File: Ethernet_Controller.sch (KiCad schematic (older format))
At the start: 45 parts, among them J1 WE-RJ45_7499111121A, T1 749020010A, U1 RTL8111H, Y1 ECS-1618-250-BN-TR

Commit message: Add review comments
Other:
- note added: "Ethernet connector have built in magnetics. \nIs using separate transformer intentional?\nUse connector without magnetics or change to connector \nwith magnetics and POE"
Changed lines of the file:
@@
 Text Label 6600 8400 2    50   ~ 0
 ETH_1V0
+Text Notes 6600 900  0    50   ~ 0
+Ethernet connector have built in magnetics. \nIs using separate transformer intentional?\nUse connector without magnetics or change to connector \nwith magnetics and POE
 $EndSCHEMATC

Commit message: fixed clock connections
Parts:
- removed C10, C9: C_10p_0402, antmicro-footprints:0402-cap, symbol antmicroCapacitors0402:C_10p_0402
- removed R17: R_1M0_0402, antmicro-footprints:0402-res, symbol antmicroResistors0402:R_1M0_0402
- removed Y1: ECS-1618-250-BN-TR, antmicro-footprints:OSC_ECS-1618-250-BN-TR, symbol antmicroOscillators:ECS-1618-250-BN-TR
- added C? (x2): C_10p_0402, antmicro-footprints:0402-cap, symbol antmicroCapacitors0402:C_10p_0402
- added R?: R_1M0_0402, antmicro-footprints:0402-res, symbol antmicroResistors0402:R_1M0_0402
- added Y?: ABM8G-25.000MHZ-18-D2Y-T, antmicro-footprints:KX-7, symbol antmicroCrystals:ABM8G-25.000MHZ-18-D2Y-T
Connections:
- wire segments 184 -> 185
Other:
- note removed: "Review Oscillator connection."
- note removed: "Why is this 1M resistor here? \n"
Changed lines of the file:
@@
 Text Notes 1600 950  0    50   ~ 0
 Choke is on secondary side.\n(Where only data is passed through)
-Wire Wire Line
-	6800 4600 6350 4600
-Wire Wire Line
-	6350 4600 6350 4450
-Wire Wire Line
-	8400 4800 8400 4950
-$Comp
-L power:GND #PWR07
-U 1 1 6199D143
-P 8400 4950
-F 0 "#PWR07" H 8400 4700 50  0001 C CNN
-F 1 "GND" H 8405 4777 50  0000 C CNN
-F 2 "" H 8400 4950 50  0001 C CNN
-F 3 "" H 8400 4950 50  0001 C CNN
-	1    8400 4950
-	1    0    0    -1
-$EndComp
 $Comp
 L antmicroResistors0402:R_1k_0402 R10
@@
 PCIE1_RX_N
 $Comp
-L antmicroOscillators:ECS-1618-250-BN-TR Y1
-U 1 1 61A23266
-P 7000 4200
-F 0 "Y1" H 7600 4549 50  0000 C CNN
-F 1 "ECS-1618-250-BN-TR" H 7600 4458 50  0000 C CNN
-F 2 "antmicro-footprints:OSC_ECS-1618-250-BN-TR" H 7000 4200 50  0001 C CNN
-F 3 "https://ecsxtal.com/store/pdf/ECS_1618.pdf" H 7000 4200 50  0001 C CNN
-F 4 "ECS-1618-250-BN-TR" H 7600 4367 50  0000 C CNN "MPN"
-F 5 "ECSXTAL" H 7600 4276 50  0000 C CNN "Manufacturer"
-	1    7000 4200
-	1    0    0    -1
-$EndComp
-Text Notes 9950 4750 0    50   ~ 0
-Review Oscillator connection.
-Text Label 9750 4500 0    50   ~ 0
-XTAL2
-Wire Wire Line
-	9500 4500 9750 4500
-Wire Wire Line
-	8700 4500 8950 4500
-Text Label 8700 4500 0    50   ~ 0
-XTAL1
-Wire Wire Line
-	9500 4500 9500 4550
-Connection ~ 9500 4500
-Wire Wire Line
-	9400 4500 9500 4500
-Wire Wire Line
-	8950 4500 9100 4500
-$Comp
-L antmicroResistors0402:R_1M0_0402 R17
-U 1 1 619ADB78
-P 9250 4500
-F 0 "R17" H 9250 4713 60  0000 C CNN
-F 1 "R_1M0_0402" H 9250 4350 60  0001 C CNN
-F 2 "antmicro-footprints:0402-res" H 9450 4700 60  0001 L CNN
-F 3 "" H 9250 4500 50  0001 C CNN
-F 4 "TE CONNECTIVITY" H 9450 4900 60  0001 L CNN "Manufacturer"
-F 5 "CRG0402F1M0" H 9450 4800 60  0001 L CNN "MPN"
-F 6 "1M0" H 9250 4615 50  0000 C CNN "Val"
-	1    9250 4500
-	1    0    0    -1
-$EndComp
-Wire Wire Line
-	8950 4500 8950 4550
-Connection ~ 8950 4500
-$Comp
-L power:GND #PWR011
-U 1 1 619A95EF
-P 9500 4850
-F 0 "#PWR011" H 9500 4600 50  0001 C CNN
-F 1 "GND" H 9505 4677 50  0000 C CNN
-F 2 "" H 9500 4850 50  0001 C CNN
-F 3 "" H 9500 4850 50  0001 C CNN
-	1    9500 4850
-	1    0    0    -1
-$EndComp
-$Comp
-L antmicroCapacitors0402:C_10p_0402 C10
-U 1 1 619A945F
-P 9500 4700
-F 0 "C10" H 9615 4745 60  0000 L CNN
-F 1 "C_10p_0402" H 9500 4550 60  0001 C CNN
-F 2 "antmicro-footprints:0402-cap" H 9700 4900 60  0001 L CNN
-F 3 "" H 9500 4700 50  0001 C CNN
-F 4 "MULTICOMP" H 9700 5100 60  0001 L CNN "Manufacturer"
-F 5 "MC0402N100D500CT" H 9700 5000 60  0001 L CNN "MPN"
-F 6 "10p" H 9615 4647 50  0000 L CNN "Val"
-	1    9500 4700
-	1    0    0    -1
-$EndComp
-$Comp
-L power:GND #PWR08
-U 1 1 619A53C6
-P 8950 4850
-F 0 "#PWR08" H 8950 4600 50  0001 C CNN
-F 1 "GND" H 8955 4677 50  0000 C CNN
-F 2 "" H 8950 4850 50  0001 C CNN
-F 3 "" H 8950 4850 50  0001 C CNN
-	1    8950 4850
-	1    0    0    -1
-$EndComp
-$Comp
-L antmicroCapacitors0402:C_10p_0402 C9
-U 1 1 619A5032
-P 8950 4700
-F 0 "C9" H 9065 4745 60  0000 L CNN
-F 1 "C_10p_0402" H 8950 4550 60  0001 C CNN
-F 2 "antmicro-footprints:0402-cap" H 9150 4900 60  0001 L CNN
-F 3 "" H 8950 4700 50  0001 C CNN
-F 4 "MULTICOMP" H 9150 5100 60  0001 L CNN "Manufacturer"
-F 5 "MC0402N100D500CT" H 9150 5000 60  0001 L CNN "MPN"
-F 6 "10p" H 9065 4647 50  0000 L CNN "Val"
-	1    8950 4700
-	1    0    0    -1
-$EndComp
-Wire Wire Line
-	8950 4400 8950 4500
-Text Notes 8950 4200 0    50   ~ 0
-Why is this 1M resistor here? \n
-Wire Wire Line
-	9500 3850 6800 3850
-Wire Wire Line
-	6800 3850 6800 4400
-Wire Wire Line
-	9500 3850 9500 4500
-Wire Wire Line
-	8400 4400 8950 4400
-$Comp
 L antmicroResistors0402:R_2k49_1%_0402 R5
 U 1 1 61B0F054
@@
 Text GLabel 7500 5350 1    50   Input ~ 0
 3V3
-Text GLabel 6350 4450 1    50   Input ~ 0
-1V8
 $Comp
 L antmicroInterfaceControllers:RTL8111H U1
@@
 Text Notes 6600 900  0    50   ~ 0
 Ethernet connector have built in magnetics. \nIs using separate transformer intentional?\nUse connector without magnetics or change to connector \nwith magnetics and POE
+$Comp
+L antmicroCrystals:ABM8G-25.000MHZ-18-D2Y-T Y?
+U 1 1 6246C7D0
+P 7700 4250
+F 0 "Y?" H 7550 4450 31  0000 L CNN
+F 1 "ABM8G-25.000MHZ-18-D2Y-T" H 7750 4450 31  0000 L CNN
+F 2 "antmicro-footprints:KX-7" H 9800 4250 50  0001 C CNN
+F 3 "" H 9900 4350 50  0001 C CNN
+F 4 "ABM8G-25.000MHZ-18-D2Y-T" H 7894 4219 31  0001 L CNN "MPN"
+F 5 "Abracon" H 7894 4157 31  0001 L CNN "Manufacturer"
+	1    7700 4250
+	1    0    0    -1
+$EndComp
+Wire Wire Line
+	7550 4250 7150 4250
+Wire Wire Line
+	7850 4250 8300 4250
+Text Label 7150 4250 0    50   ~ 0
+XTAL1
+Text Label 8300 4250 2    50   ~ 0
+XTAL2
+$Comp
+L antmicroCapacitors0402:C_10p_0402 C?
+U 1 1 6248C548
+P 7150 4500
+F 0 "C?" H 7265 4545 60  0000 L CNN
+F 1 "C_10p_0402" H 7150 4350 60  0001 C CNN
+F 2 "antmicro-footprints:0402-cap" H 7350 4700 60  0001 L CNN
+F 3 "" H 7150 4500 50  0001 C CNN
+F 4 "MULTICOMP" H 7350 4900 60  0001 L CNN "Manufacturer"
+F 5 "MC0402N100D500CT" H 7350 4800 60  0001 L CNN "MPN"
+F 6 "10p" H 7265 4447 50  0000 L CNN "Val"
+	1    7150 4500
+	1    0    0    -1
+$EndComp
+$Comp
+L antmicroCapacitors0402:C_10p_0402 C?
+U 1 1 6248CDDF
+P 8300 4500
+F 0 "C?" H 8415 4545 60  0000 L CNN
+F 1 "C_10p_0402" H 8300 4350 60  0001 C CNN
+F 2 "antmicro-footprints:0402-cap" H 8500 4700 60  0001 L CNN
+F 3 "" H 8300 4500 50  0001 C CNN
+F 4 "MULTICOMP" H 8500 4900 60  0001 L CNN "Manufacturer"
+F 5 "MC0402N100D500CT" H 8500 4800 60  0001 L CNN "MPN"
+F 6 "10p" H 8415 4447 50  0000 L CNN "Val"
+	1    8300 4500
+	1    0    0    -1
+$EndComp
+Wire Wire Line
+	7150 4250 7150 4350
+Wire Wire Line
+	8300 4250 8300 4350
+Wire Wire Line
+	7700 4050 7700 4000
+Wire Wire Line
+	7700 4450 7700 4700
+$Comp
+L power:GND #PWR?
+U 1 1 624B2B57
+P 7700 4800
+F 0 "#PWR?" H 7700 4550 50  0001 C CNN
+F 1 "GND" H 7705 4627 50  0000 C CNN
+F 2 "" H 7700 4800 50  0001 C CNN
+F 3 "" H 7700 4800 50  0001 C CNN
+	1    7700 4800
+	1    0    0    -1
+$EndComp
+$Comp
+L power:GND #PWR?
+U 1 1 624B3561
+P 7700 4000
+F 0 "#PWR?" H 7700 3750 50  0001 C CNN
+F 1 "GND" H 7705 3827 50  0000 C CNN
+F 2 "" H 7700 4000 50  0001 C CNN
+F 3 "" H 7700 4000 50  0001 C CNN
+	1    7700 4000
+	-1   0    0    1
+$EndComp
+Wire Wire Line
+	7150 4250 7150 3700
+Wire Wire Line
+	7150 3700 7550 3700
+Wire Wire Line
+	8300 3700 8300 4250
+Connection ~ 7150 4250
+Connection ~ 8300 4250
+$Comp
+L antmicroResistors0402:R_1M0_0402 R?
+U 1 1 624BEECF
+P 7700 3700
+F 0 "R?" H 7700 3900 60  0000 C CNN
+F 1 "R_1M0_0402" H 7700 3550 60  0001 C CNN
+F 2 "antmicro-footprints:0402-res" H 7900 3900 60  0001 L CNN
+F 3 "" H 7700 3700 50  0001 C CNN
+F 4 "TE CONNECTIVITY" H 7900 4100 60  0001 L CNN "Manufacturer"
+F 5 "CRG0402F1M0" H 7900 4000 60  0001 L CNN "MPN"
+F 6 "1M0" H 7700 3800 50  0000 C CNN "Val"
+F 7 "DNP" H 7700 3700 50  0000 C CNN "DNP"
+	1    7700 3700
+	1    0    0    -1
+$EndComp
+Wire Wire Line
+	7850 3700 8300 3700
+Wire Wire Line
+	7150 4650 7150 4700
+Wire Wire Line
+	7150 4700 7700 4700
+Connection ~ 7700 4700
+Wire Wire Line
+	7700 4700 7700 4800
+Wire Wire Line
+	7700 4700 8300 4700
+Wire Wire Line
+	8300 4700 8300 4650
 $EndSCHEMATC

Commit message: annotations
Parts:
- gave numbers to parts that had none: 16
- renumbered C5 to C11, C6 to C13, C7 to C14, C8 to C16, C2 to C7, C3 to C8, C4 to C9, R9 to R10, R10 to R11, R11 to R12, R12 to R13, R13 to R14, R14 to R16, R15 to R17, R16 to R18, R6 to R7, R7 to R8, R8 to R9

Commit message: Add local libs to fix CI
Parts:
- C1, C13: footprint antmicro-footprints:1210-cap -> sa800u-baseboard-hw-footprints:1210-cap; symbol antmicroCapacitorsmisc:C_1n_1210_2kV -> sa800u-baseboard-hw:C_1n_1210_2kV
- C10, C12, C15, C17, C18, C2, C3, C6, C7, C8: footprint antmicro-footprints:0402-cap -> sa800u-baseboard-hw-footprints:0402-cap; symbol antmicroCapacitors0402:C_100n_0402 -> sa800u-baseboard-hw:C_100n_0402
- C11, C14, C16, C9: footprint antmicro-footprints:0402-cap -> sa800u-baseboard-hw-footprints:0402-cap; symbol antmicroCapacitors0402:C_10n_0402 -> sa800u-baseboard-hw:C_10n_0402
- C19: footprint antmicro-footprints:0402-cap -> sa800u-baseboard-hw-footprints:0402-cap; symbol antmicroCapacitors0402:C_1u_0402 -> sa800u-baseboard-hw:C_1u_0402
- C20, C21: footprint antmicro-footprints:0402-cap -> sa800u-baseboard-hw-footprints:0402-cap; symbol antmicroCapacitors0402:C_10p_0402 -> sa800u-baseboard-hw:C_10p_0402
- C4, C5: footprint antmicro-footprints:0402-cap -> sa800u-baseboard-hw-footprints:0402-cap; symbol antmicroCapacitors0402:C_4u7_0402 -> sa800u-baseboard-hw:C_4u7_0402
- D1, D2: footprint antmicro-footprints:SOT-23-3 -> sa800u-baseboard-hw-footprints:SOT-23-3; symbol antmicroDiodesZenerSingle:BZX84C6V2LT1G -> sa800u-baseboard-hw:BZX84C6V2LT1G
- J1: footprint antmicro-footprints:7499111121A -> sa800u-baseboard-hw-footprints:7499111121A; symbol antmicroModularConnectorsJacksWithMagnetics:WE-RJ45_7499111121A -> sa800u-baseboard-hw:WE-RJ45_7499111121A
- R1, R10, R2, R3, R4, R7, R8, R9: footprint antmicro-footprints:0402-res -> sa800u-baseboard-hw-footprints:0402-res; symbol antmicroResistors0402:R_75R_0402 -> sa800u-baseboard-hw:R_75R_0402
- R11, R14: footprint antmicro-footprints:0402-res -> sa800u-baseboard-hw-footprints:0402-res; symbol antmicroResistors0402:R_1k_0402 -> sa800u-baseboard-hw:R_1k_0402
- R12, R13: footprint antmicro-footprints:0402-res -> sa800u-baseboard-hw-footprints:0402-res; symbol antmicroResistors0402:R_10k_0402 -> sa800u-baseboard-hw:R_10k_0402
- R15: footprint antmicro-footprints:0402-res -> sa800u-baseboard-hw-footprints:0402-res; symbol antmicroResistors0402:R_1M0_0402 -> sa800u-baseboard-hw:R_1M0_0402
- R16: footprint antmicro-footprints:0603-res -> sa800u-baseboard-hw-footprints:0603-res; symbol antmicroResistors0603:R_15k_0603 -> sa800u-baseboard-hw:R_15k_0603
- R17, R18: footprint antmicro-footprints:0402-res -> sa800u-baseboard-hw-footprints:0402-res; symbol antmicroResistors0402:R_470R_0402 -> sa800u-baseboard-hw:R_470R_0402
- R5: footprint antmicro-footprints:0402-res -> sa800u-baseboard-hw-footprints:0402-res; symbol antmicroResistors0402:R_2k49_1%_0402 -> sa800u-baseboard-hw:R_2k49_1%_0402
- R6: footprint antmicro-footprints:0402-res -> sa800u-baseboard-hw-footprints:0402-res; symbol antmicroResistors0402:R_0R_0402 -> sa800u-baseboard-hw:R_0R_0402
- T1: footprint antmicro-footprints:749020010A -> sa800u-baseboard-hw-footprints:749020010A; symbol antmicroInterfaceDriversReceiversTransceivers:749020010A -> sa800u-baseboard-hw:749020010A
- U1: footprint antmicro-footprints:RTL8111H -> sa800u-baseboard-hw-footprints:RTL8111H; symbol antmicroInterfaceControllers:RTL8111H -> sa800u-baseboard-hw:RTL8111H
- Y1: footprint antmicro-footprints:KX-7 -> sa800u-baseboard-hw-footprints:KX-7; symbol antmicroCrystals:ABM8G-25.000MHZ-18-D2Y-T -> sa800u-baseboard-hw:ABM8G-25.000MHZ-18-D2Y-T

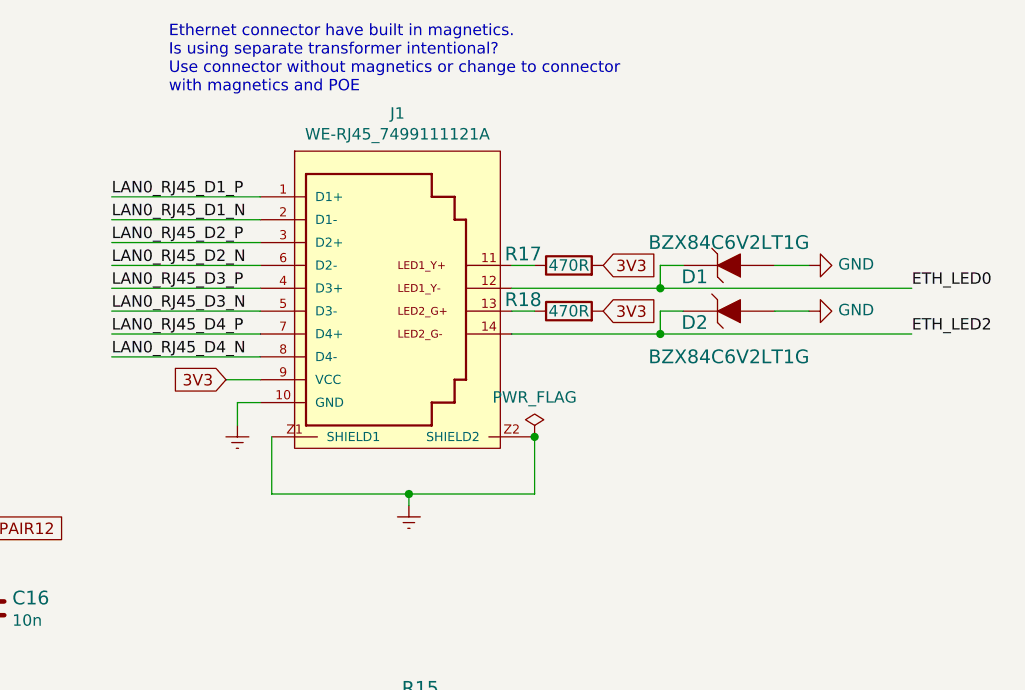
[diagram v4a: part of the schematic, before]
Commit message: add rj45 without trafo
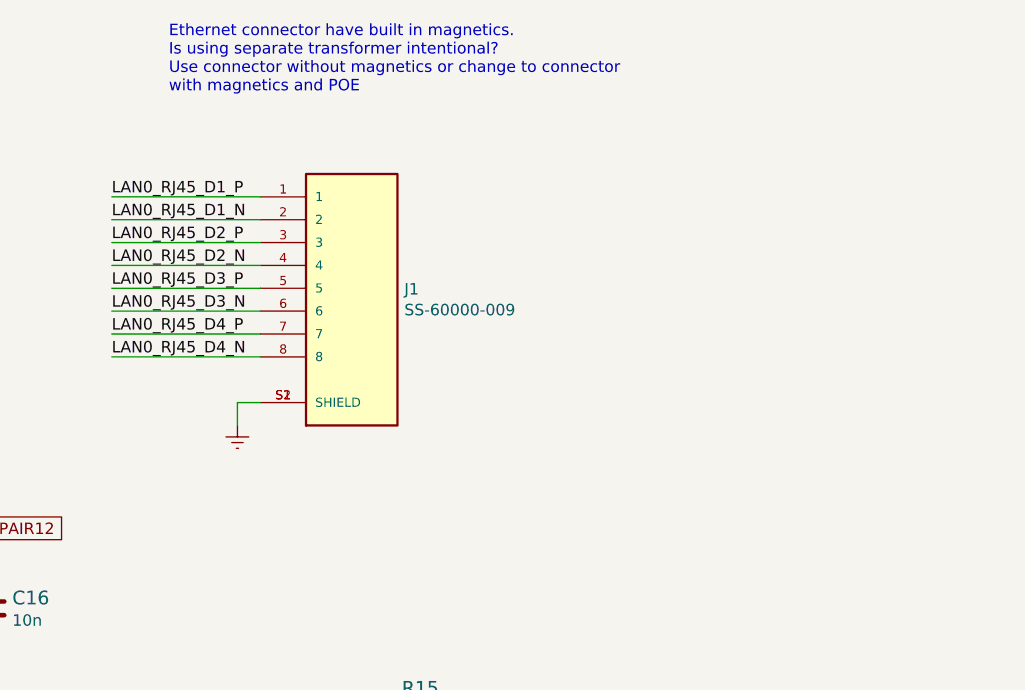
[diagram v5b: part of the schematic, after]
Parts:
- removed D1, D2: BZX84C6V2LT1G, sa800u-baseboard-hw-footprints:SOT-23-3, symbol sa800u-baseboard-hw:BZX84C6V2LT1G
- removed J1: WE-RJ45_7499111121A, sa800u-baseboard-hw-footprints:7499111121A, symbol sa800u-baseboard-hw:WE-RJ45_7499111121A
- removed R17, R18: R_470R_0402, sa800u-baseboard-hw-footprints:0402-res, symbol sa800u-baseboard-hw:R_470R_0402
- added J1: SS-60000-009, antmicro-footprints:BEL_SS-60000-009, symbol antmicroModularConnectorsJacks:SS-60000-009
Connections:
- net Earth: now also J1.S1 (SHIELD), J1.S2 (SHIELD)
- net LAN0_RJ45_D1_N: now also J1.2
- net LAN0_RJ45_D1_P: now also J1.1
- net LAN0_RJ45_D2_N: now also J1.4
- net LAN0_RJ45_D2_P: now also J1.3
- net LAN0_RJ45_D3_N: now also J1.6
- net LAN0_RJ45_D3_P: now also J1.5
- net LAN0_RJ45_D4_N: now also J1.8
- net LAN0_RJ45_D4_P: now also J1.7
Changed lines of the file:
@@
 	2050 2100 2800 2100
-Wire Wire Line
-	9250 1850 9400 1850
-Wire Wire Line
-	9250 1650 9400 1650
-Wire Wire Line
-	8200 2650 8200 2400
-Wire Wire Line
-	7050 2400 7050 2650
-Text GLabel 6850 2150 0    50   Input ~ 0
-3V3
-Text Label 9850 1950 0    50   ~ 0
-ETH_LED2
-$Comp
-L sa800u-baseboard-hw:BZX84C6V2LT1G D2
-U 1 1 61991971
-P 9050 1850
-F 0 "D2" H 9200 1900 60  0000 C CNN
-F 1 "BZX84C6V2LT1G" H 9050 2050 60  0000 C CNN
-F 2 "sa800u-baseboard-hw-footprints:SOT-23-3" H 9250 2050 60  0001 L CNN
-F 3 "https://www.onsemi.com/pdf/datasheet/bzx84c2v4lt1-d.pdf" H 9250 2150 60  0001 L CNN
-F 4 "BZX84C6V2LT1G" H 9250 2350 60  0001 L CNN "MPN"
-F 5 "ON Semiconductor" H 9250 2950 60  0001 L CNN "Manufacturer"
-	1    9050 1850
-	-1   0    0    1
-$EndComp
-Connection ~ 8750 1750
-Wire Wire Line
-	8750 1650 8750 1750
-Wire Wire Line
-	8850 1650 8750 1650
-Wire Wire Line
-	8100 1750 8750 1750
-Wire Wire Line
-	8750 1850 8850 1850
-Wire Wire Line
-	8750 1950 8750 1850
-Wire Wire Line
-	8100 1950 8750 1950
-Text GLabel 8500 1850 2    50   Input ~ 0
-3V3
-Text GLabel 8500 1650 2    50   Input ~ 0
-3V3
-$Comp
-L sa800u-baseboard-hw:BZX84C6V2LT1G D1
-U 1 1 61976A91
-P 9050 1650
-F 0 "D1" H 9200 1700 60  0000 C CNN
-F 1 "BZX84C6V2LT1G" H 9050 1550 60  0000 C CNN
-F 2 "sa800u-baseboard-hw-footprints:SOT-23-3" H 9250 1850 60  0001 L CNN
-F 3 "https://www.onsemi.com/pdf/datasheet/bzx84c2v4lt1-d.pdf" H 9250 1950 60  0001 L CNN
-F 4 "BZX84C6V2LT1G" H 9250 2150 60  0001 L CNN "MPN"
-F 5 "ON Semiconductor" H 9250 2750 60  0001 L CNN "Manufacturer"
-	1    9050 1650
-	-1   0    0    1
-$EndComp
-Wire Wire Line
-	8200 1850 8100 1850
-Text Label 9850 1750 0    50   ~ 0
-ETH_LED0
-Wire Wire Line
-	8100 1650 8200 1650
-$Comp
-L sa800u-baseboard-hw:R_470R_0402 R17
-U 1 1 6196D91A
-P 8350 1650
-F 0 "R17" H 8150 1700 60  0000 C CNN
-F 1 "R_470R_0402" H 8350 1500 60  0001 C CNN
-F 2 "sa800u-baseboard-hw-footprints:0402-res" H 8550 1850 60  0001 L CNN
-F 3 "" H 8350 1650 50  0001 C CNN
-F 4 "VISHAY" H 8550 2050 60  0001 L CNN "Manufacturer"
-F 5 "CRCW0402470RFKED" H 8550 1950 60  0001 L CNN "MPN"
-F 6 "470R" H 8350 1650 50  0000 C CNN "Val"
-	1    8350 1650
-	1    0    0    -1
-$EndComp
-$Comp
-L sa800u-baseboard-hw:R_470R_0402 R18
-U 1 1 619694FE
-P 8350 1850
-F 0 "R18" H 8150 1900 60  0000 C CNN
-F 1 "R_470R_0402" H 8350 1700 60  0001 C CNN
-F 2 "sa800u-baseboard-hw-footprints:0402-res" H 8550 2050 60  0001 L CNN
-F 3 "" H 8350 1850 50  0001 C CNN
-F 4 "VISHAY" H 8550 2250 60  0001 L CNN "Manufacturer"
-F 5 "CRCW0402470RFKED" H 8550 2150 60  0001 L CNN "MPN"
-F 6 "470R" H 8350 1850 50  0000 C CNN "Val"
-	1    8350 1850
-	1    0    0    -1
-$EndComp
 Wire Wire Line
 	7000 2050 6350 2050
@@
 Text Label 6350 1350 0    50   ~ 0
 LAN0_RJ45_D1_P
-$Comp
-L sa800u-baseboard-hw:WE-RJ45_7499111121A J1
-U 1 1 61953706
-P 7500 1850
-F 0 "J1" H 7600 2715 50  0000 C CNN
-F 1 "WE-RJ45_7499111121A" H 7600 2624 50  0000 C CNN
-F 2 "sa800u-baseboard-hw-footprints:7499111121A" H 7500 1850 50  0001 L BNN
-F 3 "" H 7500 1850 50  0001 L BNN
-F 4 "7499111121A" H 7500 1850 50  0001 L BNN "MPN"
-F 5 "WURTH ELEKTRONIK" H 7500 1850 50  0001 C CNN "Manufacturer"
-	1    7500 1850
-	1    0    0    -1
-$EndComp
 Wire Wire Line
 	6900 2250 7000 2250
-Wire Wire Line
-	6850 2150 7000 2150
 Wire Wire Line
 	4600 2400 4600 3000
@@
 $EndComp
 Wire Wire Line
-	8750 1950 9850 1950
-Connection ~ 8750 1950
-Wire Wire Line
-	8750 1750 9850 1750
-Wire Wire Line
 	2800 1200 1900 1200
 Wire Wire Line
@@
 Wire Wire Line
 	2050 1500 2800 1500
-$Comp
-L sa800u-baseboard-hw:GND #PWR011
-U 1 1 61C7BBCB
-P 9400 1650
-F 0 "#PWR011" H 9400 1400 50  0001 C CNN
-F 1 "GND" V 9405 1522 50  0000 R CNN
-F 2 "" H 9400 1650 50  0001 C CNN
-F 3 "" H 9400 1650 50  0001 C CNN
-	1    9400 1650
-	0    -1   -1   0
-$EndComp
-$Comp
-L sa800u-baseboard-hw:GND #PWR012
-U 1 1 61C7BF66
-P 9400 1850
-F 0 "#PWR012" H 9400 1600 50  0001 C CNN
-F 1 "GND" V 9405 1722 50  0000 R CNN
-F 2 "" H 9400 1850 50  0001 C CNN
-F 3 "" H 9400 1850 50  0001 C CNN
-	1    9400 1850
-	0    -1   -1   0
-$EndComp
 Text Notes 950  4950 0    50   ~ 0
 Consider separating PSU for analog / digital
@@
 	1    0    0    -1
 $EndComp
-$Comp
-L sa800u-baseboard-hw:Earth #PWR07
-U 1 1 619F3D25
-P 7650 2700
-F 0 "#PWR07" H 7650 2450 50  0001 C CNN
-F 1 "Earth" H 7650 2550 50  0001 C CNN
-F 2 "" H 7650 2700 50  0001 C CNN
-F 3 "~" H 7650 2700 50  0001 C CNN
-	1    7650 2700
-	1    0    0    -1
-$EndComp
-Wire Wire Line
-	7050 2650 7650 2650
-Wire Wire Line
-	7650 2700 7650 2650
-Connection ~ 7650 2650
-Wire Wire Line
-	7650 2650 8200 2650
 Wire Wire Line
 	6900 2250 6900 2350
@@
 	1    0    0    -1
 $EndComp
-$Comp
-L sa800u-baseboard-hw:PWR_FLAG #FLG01
-U 1 1 62B8658A
-P 8200 2400
-F 0 "#FLG01" H 8200 2475 50  0001 C CNN
-F 1 "PWR_FLAG" H 8200 2573 50  0000 C CNN
-F 2 "" H 8200 2400 50  0001 C CNN
-F 3 "~" H 8200 2400 50  0001 C CNN
-	1    8200 2400
-	1    0    0    -1
-$EndComp
-Connection ~ 8200 2400
 Text Label 2000 5700 0    50   ~ 0
 ETH_1V0
@@
 Wire Wire Line
 	8300 4700 8300 4650
+$Comp
+L antmicroModularConnectorsJacks:SS-60000-009 J1
+U 1 1 61EEF185
+P 7400 1750
+F 0 "J1" H 7630 1746 50  0000 L CNN
+F 1 "SS-60000-009" H 7630 1655 50  0000 L CNN
+F 2 "antmicro-footprints:BEL_SS-60000-009" H 7400 1750 50  0001 C CNN
+F 3 "https://www.farnell.com/datasheets/2615305.pdf" H 7400 1750 50  0001 C CNN
+F 4 "SS-60000-009" H 7400 1750 50  0001 C CNN "MPN"
+F 5 "STEWART CONNECTOR" H 7400 1750 50  0001 C CNN "Manufacturer"
+	1    7400 1750
+	1    0    0    -1
+$EndComp
 $EndSCHEMATC
